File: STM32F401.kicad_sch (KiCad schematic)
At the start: 31 parts, among them J1 Conn_02x10_Odd_Even, J2 Conn_02x10_Odd_Even, J3 POWER, J4 USB_B_Micro, J5 Conn_01x04, U1 AMS1117-3.3, U2 STM32F401RCTx

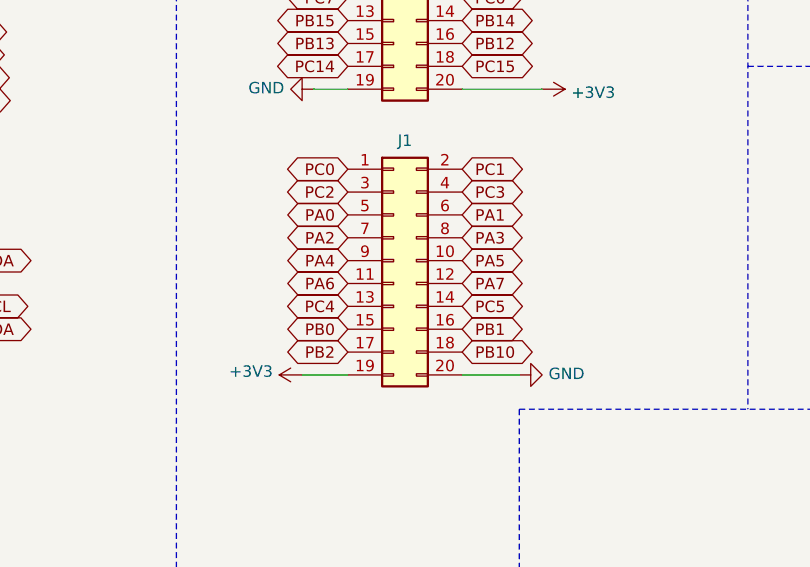
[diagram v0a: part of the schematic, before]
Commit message: added circuitry for magnetometer, gyroscope and h-bridges
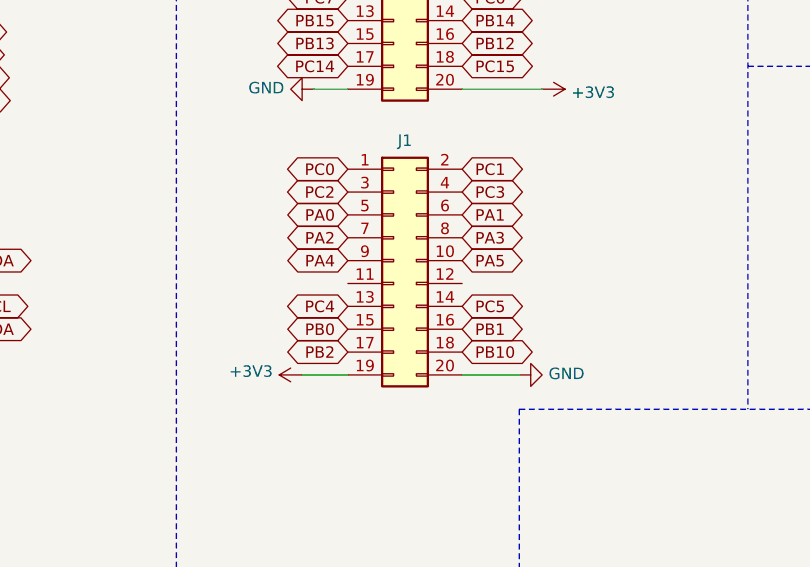
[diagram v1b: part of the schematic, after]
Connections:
- net PA6: no longer J1.11 (Pin_11)
- net PA7: no longer J1.12 (Pin_12)
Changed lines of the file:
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@@
-		)
-	)
-	(global_label "PA6"
-		(shape bidirectional)
-		(at 156.21 151.13 180)
-		(effects
-			(font
-				(size 1.27 1.27)
-			)
-			(justify right)
-		)
-		(property "Intersheetrefs" "${INTERSHEET_REFS}"
-			(at 156.21 151.13 0)
-			(hide yes)
-			(show_name no)
-			(do_not_autoplace no)
-			(effects
-				(font
-					(size 1.27 1.27)
-				)
-			)
 		)
 	)
@@
 			(hide yes)
 			(show_name no)
-			(do_not_autoplace no)
-			(effects
-				(font
-					(size 1.27 1.27)
-				)
-			)
-		)
-	)
-	(global_label "PA7"
-		(shape bidirectional)
-		(at 168.91 151.13 0)
-		(effects
-			(font
-				(size 1.27 1.27)
-			)
-			(justify left)
-		)
-		(property "Intersheetrefs" "${INTERSHEET_REFS}"
-			(at 168.91 151.13 0)
-			(hide yes)
-			(show_name no)
